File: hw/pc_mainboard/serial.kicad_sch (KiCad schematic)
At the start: 1 part, among them U4 CP2102N-A02-GQFN20

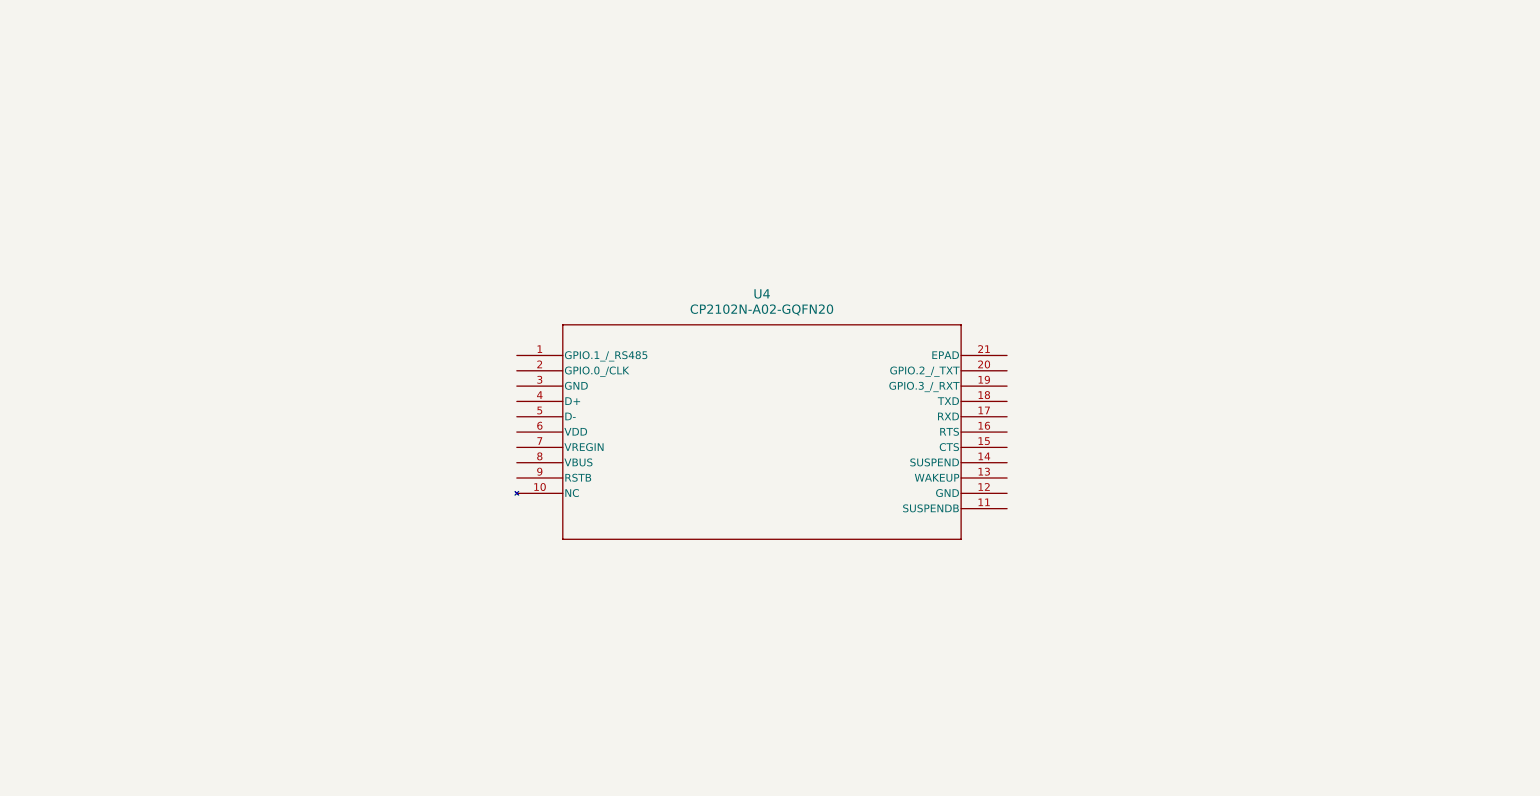
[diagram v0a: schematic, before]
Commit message: Added serial schematic capture
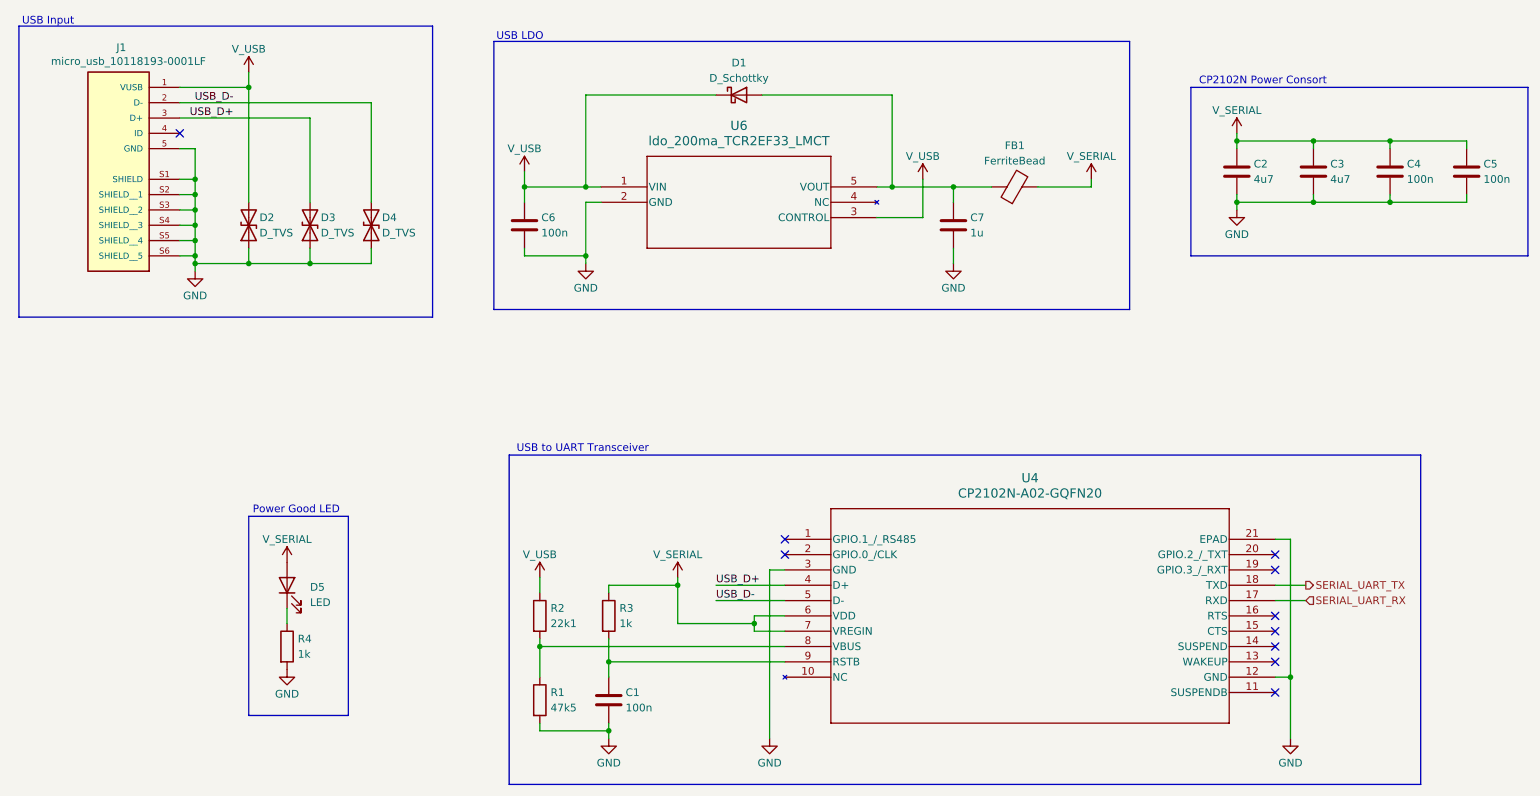
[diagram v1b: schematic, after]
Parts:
- added C1, C4, C5, C6: 100n, symbol Device:C
- added C2, C3: 4u7, symbol Device:C
- added C7: 1u, symbol Device:C
- added D1: D_Schottky, symbol Device:D_Schottky
- added D2, D3, D4: D_TVS, symbol Device:D_TVS
- added D5: LED, symbol Device:LED
- added FB1: FerriteBead, symbol Device:FerriteBead
- added J1: micro_usb_10118193-0001LF, 10118193-0001LF:AMPHENOL_10118193-0001LF, symbol pc_mainboard:micro_usb_10118193-0001LF
- added R1: 47k5, symbol Device:R
- added R2: 22k1, symbol Device:R
- added R3, R4: 1k, symbol Device:R
- added U6: ldo_200ma_TCR2EF33_LMCT, SOT-25 SMV_TOS, symbol pc_mainboard:ldo_200ma_TCR2EF33_LMCT
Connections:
- net GND: now reaches U4.12 (GND)
- net GND: now also U4.21 (EPAD), U4.3 (GND), C1.2, C2.2, C3.2, C4.2, C5.2, C6.2, C7.2, D2.1 (A1), D3.1 (A1), D4.1 (A1), J1.5 (GND), J1.S1 (SHIELD), J1.S2 (SHIELD__1), J1.S3 (SHIELD__2), J1.S4 (SHIELD__3), J1.S5 (SHIELD__4), J1.S6 (SHIELD__5), R1.2, R4.2, U6.2 (GND)
- net SERIAL_UART_RX: now reaches U4.17 (RXD)
- net SERIAL_UART_TX: now reaches U4.18 (TXD)
- net USB_D+: now reaches U4.4 (D+)
- net USB_D+: now also D3.2 (A2), J1.3 (D+)
- net USB_D-: now reaches U4.5 (D-)
- net USB_D-: now also D4.2 (A2), J1.2 (D-)
- net V_SERIAL: now reaches U4.6 (VDD)
- net V_SERIAL: now also U4.7 (VREGIN), C2.1, C3.1, C4.1, C5.1, D5.2 (A), FB1.2, R3.1
- net at U4.8 (VBUS): now also R1.1, R2.2
- net at U4.9 (RSTB): now also C1.1, R3.2
- new net: C7.1, D1.2 (A), FB1.1, U6.5 (VOUT)
- new net: D5.1 (K), R4.1
- new net V_USB: C6.1, D1.1 (K), D2.2 (A2), J1.1 (VUSB), R2.1, U6.1 (VIN), U6.3 (CONTROL)
- no-connect marks 0 -> 10
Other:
- note added: "CP2102N Power Consort"
- note added: "Power Good LED"
- note added: "USB Input"
- note added: "USB LDO"
- note added: "USB to UART Transceiver"
- moved on the sheet: U4
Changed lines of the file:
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@@
 		(title "Serial")
 	)
-	(symbol
-		(lib_id "pc_mainboard:CP2102N-A02-GQFN20")
-		(at 104.14 82.55 0)
-		(unit 1)
-		(exclude_from_sim no)
-		(in_bom yes)
-		(on_board yes)
-		(dnp no)
-		(fields_autoplaced yes)
-		(property "Reference" "U4"
-			(at 144.78 72.39 0)
-			(effects
-				(font
-					(size 1.524 1.524)
-				)
-			)
-		)
-		(property "Value" "CP2102N-A02-GQFN20"
-			(at 144.78 74.93 0)
-			(effects
-				(font
-					(size 1.524 1.524)
-				)
-			)
-		)
-		(property "Footprint" "QFN20_CP2102N_SIL"
-			(at 104.14 82.55 0)
-			(effects
-				(font
-					(size 1.27 1.27)
-					(italic yes)
-				)
-				(hide yes)
-			)
-		)
-		(property "Datasheet" "CP2102N-A02-GQFN20"
-			(at 104.14 82.55 0)
-			(effects
-				(font
-					(size 1.27 1.27)
-					(italic yes)
-				)
-				(hide yes)
-			)
-		)
-		(property "Description" ""
-			(at 104.14 82.55 0)
-			(effects
-				(font
-					(size 1.27 1.27)
-				)
-				(hide yes)
-			)
-		)
-		(pin "3"
-		)
-		(pin "9"
-		)
-		(pin "16"
-		)
-		(pin "4"
-		)
-		(pin "5"
-		)
-		(pin "20"
-		)
-		(pin "18"
-		)
-		(pin "7"
-		)
-		(pin "8"
-		)
-		(pin "6"
-		)
-		(pin "17"
-		)
-		(pin "15"
-		)
-		(pin "14"
-		)
-		(pin "13"
-		)
-		(pin "12"
-		)
-		(pin "11"
-		)
-		(pin "1"
-		)
-		(pin "10"
-		)
-		(pin "21"
-		)
-		(pin "19"
-		)
-		(pin "2"
-		)
-		(instances
-			(project ""
-				(path "/69a74940-cd00-4a75-bd5b-2bda9e86219a/ca84e111-cd01-464e-9a8f-53a5482dcbab"
-					(reference "U4")
-					(unit 1)
-				)
-			)
-		)
-	)
-)

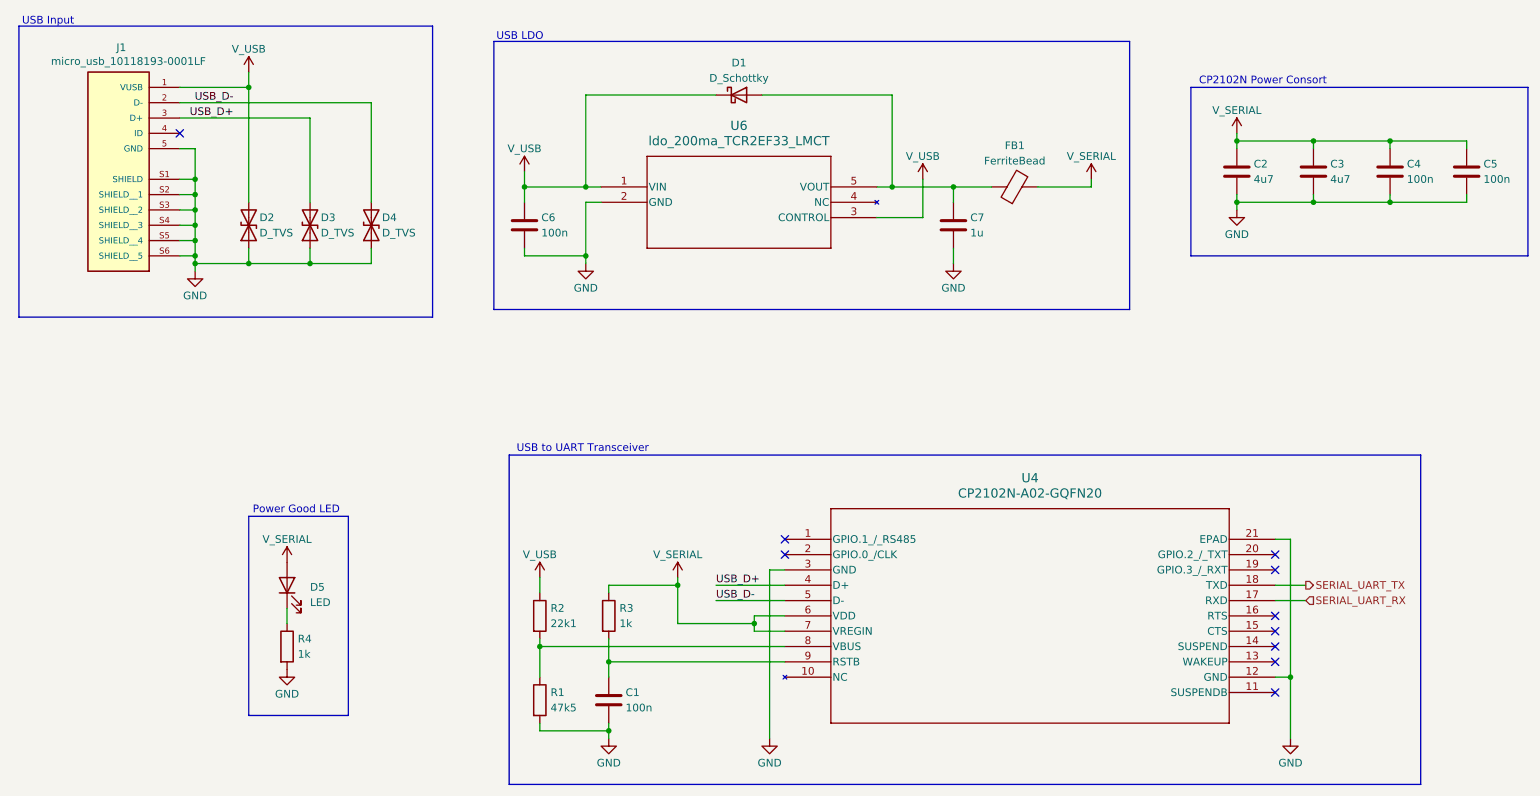
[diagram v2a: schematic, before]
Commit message: SD card research, updated some formatting (#49)
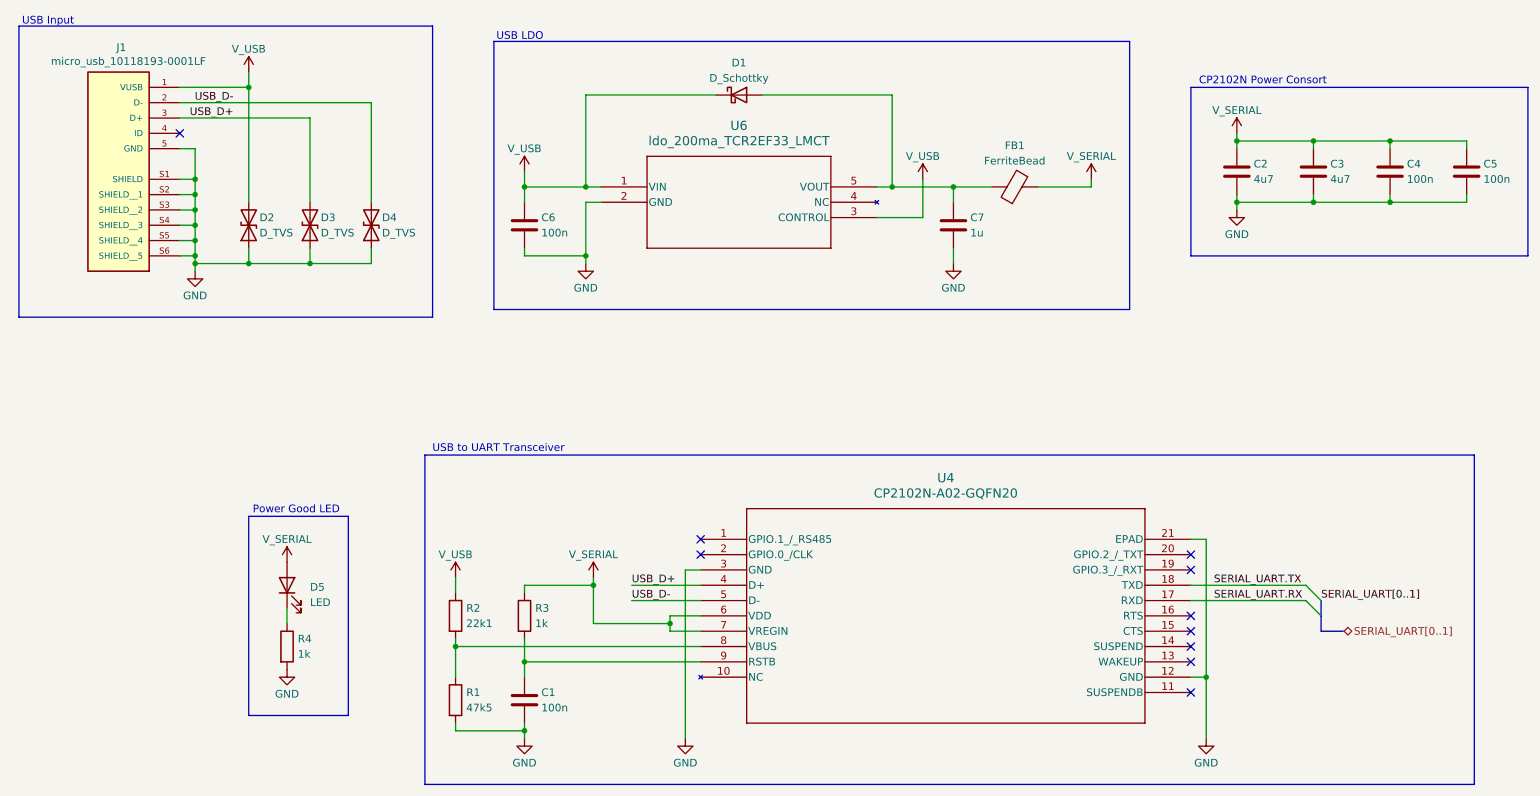
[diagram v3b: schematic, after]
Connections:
- net SERIAL_UART_RX renamed SERIAL_UART.RX
- net SERIAL_UART_TX renamed SERIAL_UART.TX
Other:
- moved on the sheet: C1, R1, R2, R3, U4
